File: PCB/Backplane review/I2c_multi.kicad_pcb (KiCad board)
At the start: 2 copper layers, 52.3 x 52.3 mm, 31 parts, among them J1_EZO_DO1 Conn_01x05_Socket, J2_EZO_Ph1 Conn_01x05_Socket, J3_EZO_ORP1 Conn_01x05_Socket, J4_EZO_CO1 Conn_01x05_Socket, J5_Feather1 Conn_01x04_Pin, J5_Feather2 Conn_01x04_Pin, J6_PWR1 Conn_01x02_Pin, J7_Temp1 Conn_01x04_Pin, J8_Pres1 Conn_01x04_Pin, U1 LD1117S33TR_SOT223, U2 SIP32411DR-T1-GE3, U3 SIP32411DR-T1-GE3, U4 SIP32411DR-T1-GE3, U5 SIP32411DR-T1-GE3, U6 AT24CS64-XHM

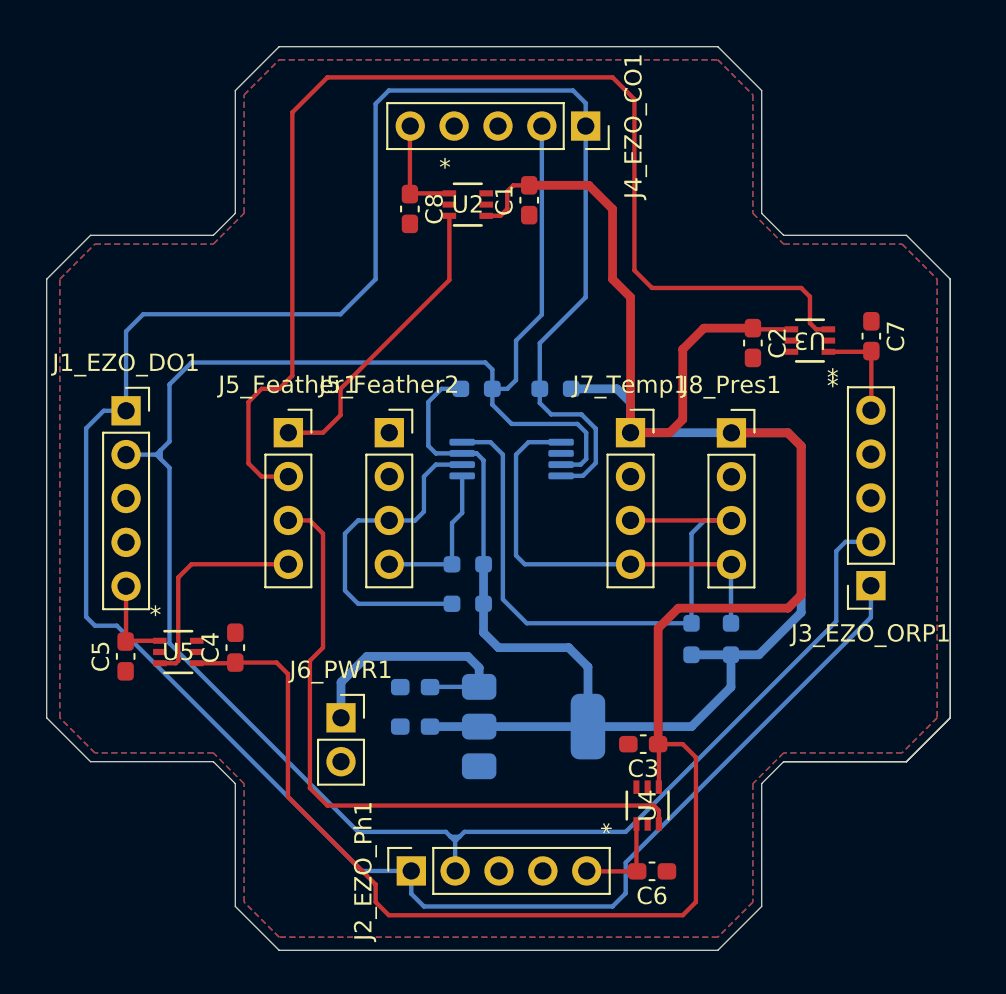
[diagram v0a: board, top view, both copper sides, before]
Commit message: Delete folder and clean Programme_Kristen Folder Modifying edgecut for the last pcb
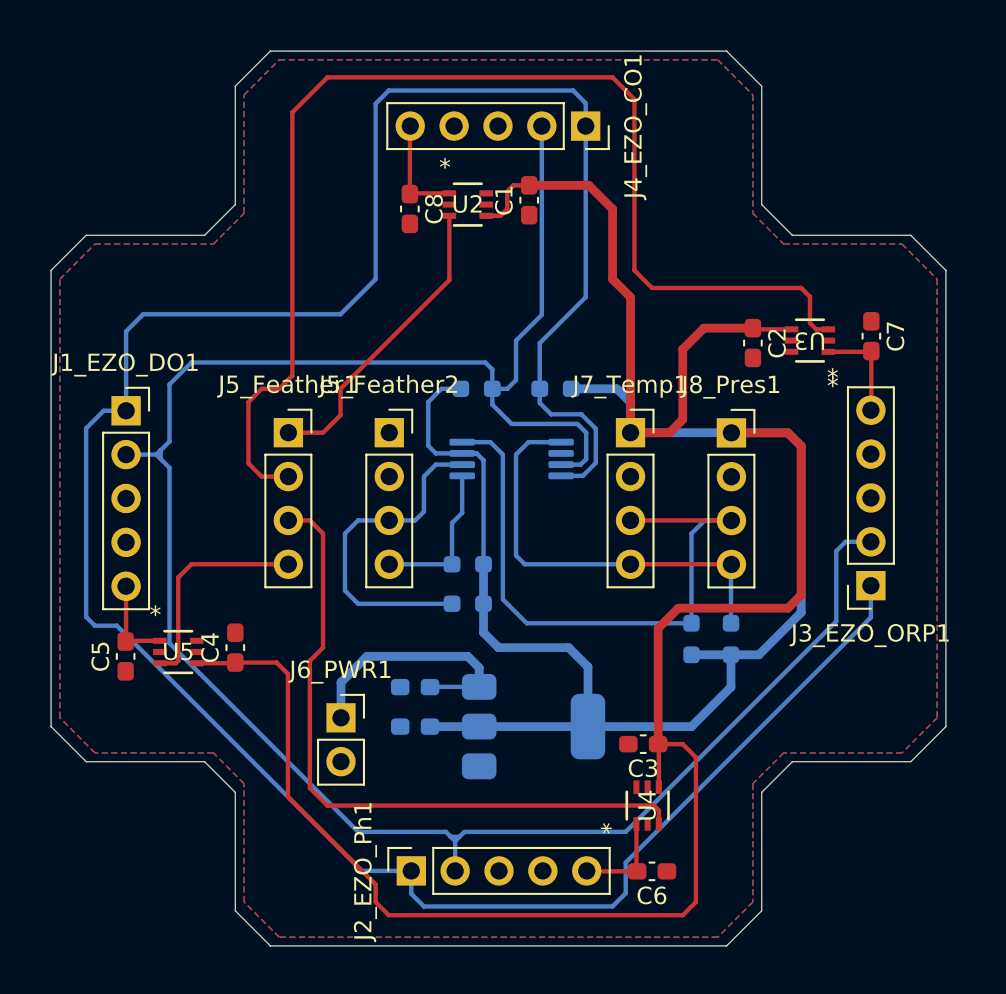
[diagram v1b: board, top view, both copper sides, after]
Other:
- board size 52.3 x 52.3 mm -> 51.8 x 51.8 mm
